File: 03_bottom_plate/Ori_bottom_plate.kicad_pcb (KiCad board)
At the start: 2 copper layers, 278.9 x 76 mm, 81 parts, among them U1 HOLE, U10 HOLE, U11 HOLE, U12 HOLE, U13 HOLE, U14 HOLE, U15 HOLE, U16 HOLE, U17 HOLE, U18 HOLE, U19 HOLE, U2 HOLE, U20 HOLE, U21 HOLE, U22 HOLE, U23 HOLE, U24 HOLE, U25 HOLE, U26 HOLE, U27 HOLE, U28 HOLE, U29 HOLE, U3 HOLE, U30 HOLE, U31 HOLE, U32 HOLE, U33 HOLE, U34 HOLE, U35 HOLE, U36 HOLE, U37 HOLE, U38 HOLE, U39 HOLE, U4 HOLE, U40 HOLE, U41 HOLE, U42 HOLE, U43 HOLE, U44 HOLE, U45 HOLE, U46 HOLE, U47 HOLE, U48 HOLE, U49 HOLE, U5 HOLE, U50 HOLE, U51 HOLE, U52 HOLE, U53 HOLE, U54 HOLE, U57 HOLE, U6 HOLE, U61 HOLE, U7 HOLE, U8 HOLE, U9 HOLE

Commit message: remove a column
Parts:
- removed H21, H22, H23: MountingHole, acheron_Hardware:MouseBite_IPC7351
- removed H24, H25: MountingHole, random-keyboard-parts:Generic-Mounthole
- removed U50, U51, U52, U54: HOLE, Keeb_footprints:MX100_outline
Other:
- board size 278.9 x 76 mm -> 253.5 x 76 mm

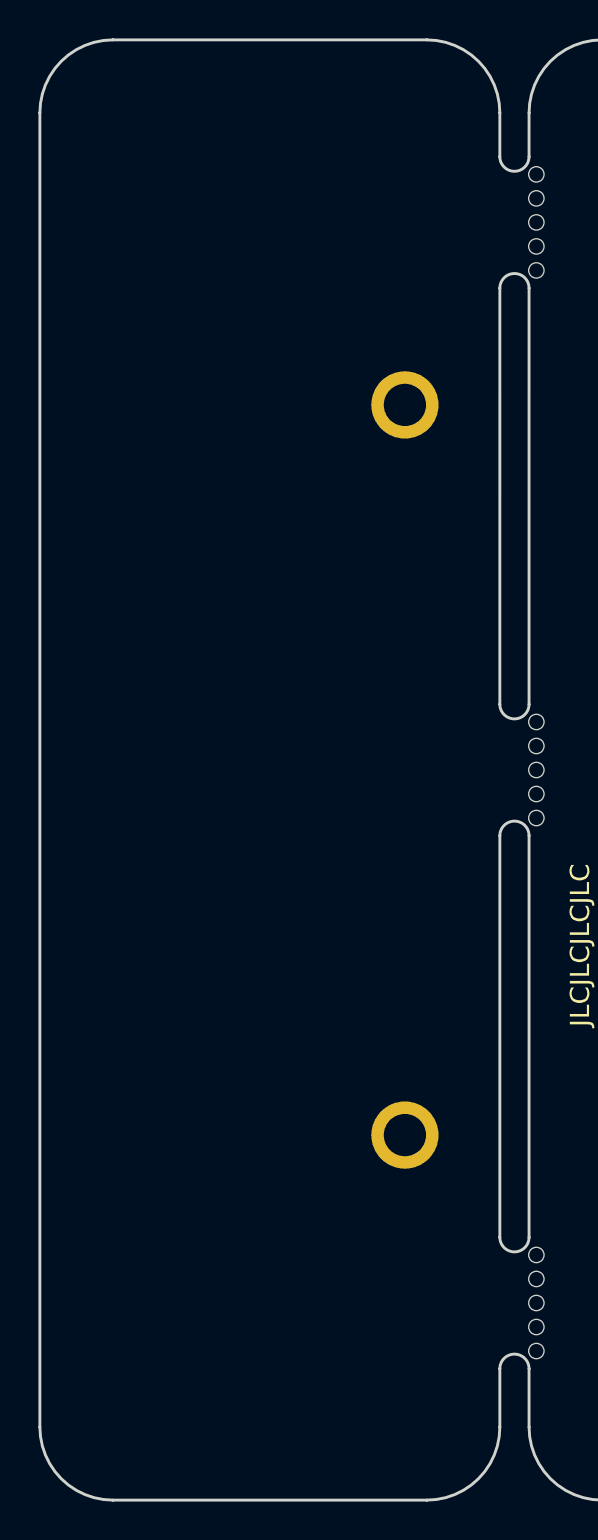
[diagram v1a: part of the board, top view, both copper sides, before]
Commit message: Moved macro column a tiny bit
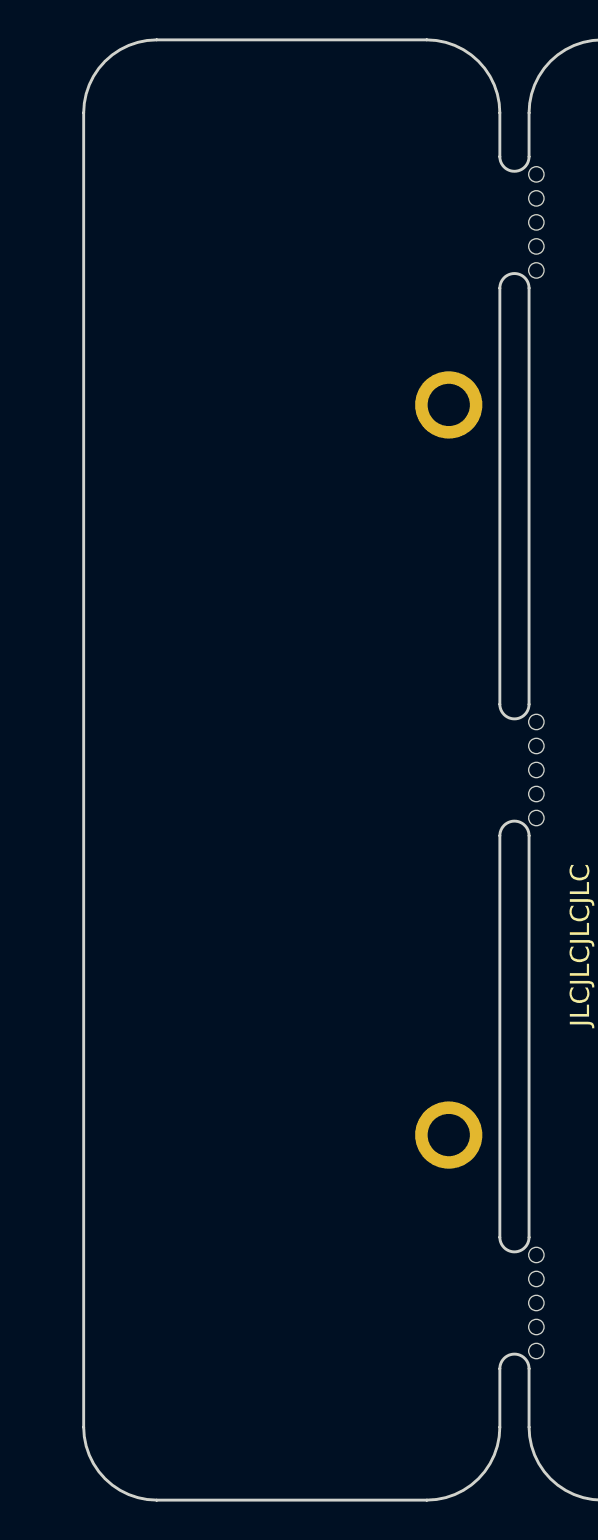
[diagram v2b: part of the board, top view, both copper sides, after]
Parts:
- moved H16 2.28 mm to (141.7, 59.7)
- moved H7 2.28 mm to (141.7, 97.7)
- moved U49 2.28 mm to (132.2, 50.2)
- moved U53 2.28 mm to (132.2, 69.2)
- moved U57 2.28 mm to (132.2, 88.2)
- moved U61 2.28 mm to (132.2, 107.2)
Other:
- board size 253.5 x 76 mm -> 251.2 x 76 mm

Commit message: 19.05mm spacing; move macro column to right side
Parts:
- removed H1, H2, H3, H4, H5, H6: MountingHole, random-keyboard-parts:Generic-Mounthole
- added D1: DIODE, Keeb_footprints:D_SOD-123_modified, F.Cu at (389.4, 59.5)
- moved U53 257.1 mm to (389.4, 69.0)
- moved U49 257.1 mm to (389.3, 50.0)
- moved U57 257.1 mm to (389.3, 88.1)
- moved U61 257.1 mm to (389.3, 107.2)
- moved H16 238.1 mm to (379.8, 59.5)
- moved H7 238.1 mm to (379.8, 97.7)
- moved H19 228.7 mm to (375.0, 107.2)
- moved H18 228.7 mm to (375.0, 50.0)
- moved H20 228.7 mm to (375.0, 78.6)
- moved H17 1.83 mm to (203.6, 50.0)
- moved U12 1.11 mm to (365.5, 50.0)
- moved U24 1.11 mm to (365.5, 69.1)
- moved U36 1.10 mm to (365.5, 88.1)
- moved U48 1.10 mm to (365.5, 107.2)
- moved U11 1.06 mm to (346.5, 50.0)
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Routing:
- net GND: track 0.00 -> 6.09 mm, vias 0 -> 2
- added copper zone on B.Cu, net GND
- added copper zone on F.Cu, net GND
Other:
- board size 251.2 x 76 mm -> 252.4 x 76.2 mm

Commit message: Updated firmware
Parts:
- added H1: MountingHole, random-keyboard-parts:Generic-Mounthole, F.Cu at (165.5, 39.9)
- added H2: MountingHole, random-keyboard-parts:Generic-Mounthole, F.Cu at (165.5, 117.3)
- added H21: MountingHole, random-keyboard-parts:Generic-Mounthole, F.Cu at (389.4, 39.9)
- added H22: MountingHole, random-keyboard-parts:Generic-Mounthole, F.Cu at (389.4, 117.3)
- added H3: MountingHole, random-keyboard-parts:Generic-Mounthole, F.Cu at (260.8, 39.9)
- added H4: MountingHole, random-keyboard-parts:Generic-Mounthole, F.Cu at (260.8, 117.3)
- added H5: MountingHole, random-keyboard-parts:Generic-Mounthole, F.Cu at (337.0, 39.9)
- added H6: MountingHole, random-keyboard-parts:Generic-Mounthole, F.Cu at (337.0, 117.3)
- moved H9 0.14 mm to (165.5, 59.5)
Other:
- board size 252.4 x 76.2 mm -> 252.4 x 82.2 mm
- rule pad_to_mask_clearance: 0.051 -> 0

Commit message: added different plate mounts
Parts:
- removed the H10 at (222.6, 59.5)
- removed the H11 at (222.6, 97.6)
- removed H12, H13, H14, H15, H16, H17, H21, H22: MountingHole, random-keyboard-parts:Generic-Mounthole
- removed the H9 at (165.5, 59.5)
- moved H8 224.7 mm to (389.4, 117.3)
- moved H7 58.6 mm to (389.4, 39.9)
- renumbered H19 to H10, H20 to H11, H18 to H9

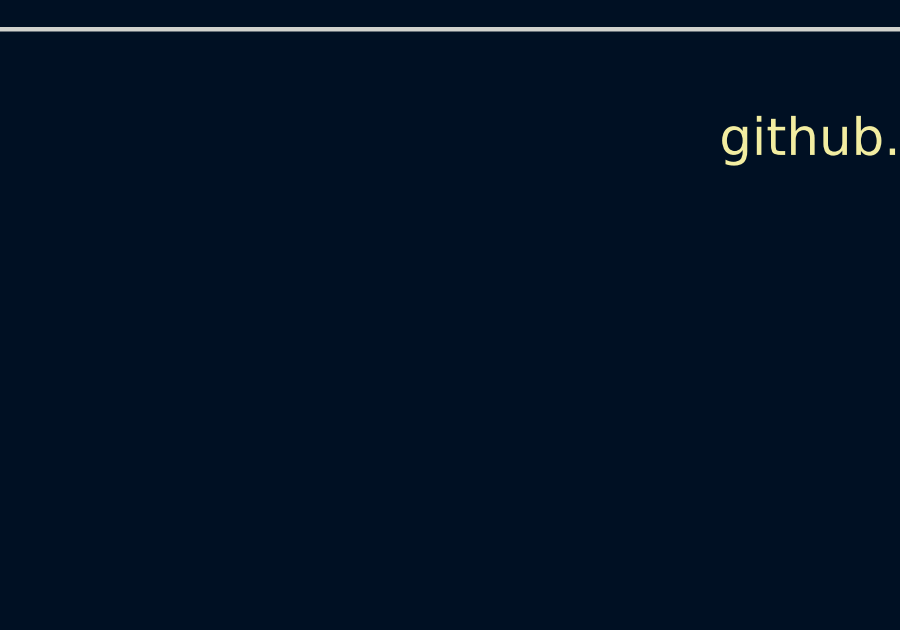
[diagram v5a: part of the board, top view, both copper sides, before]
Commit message: modify top plate
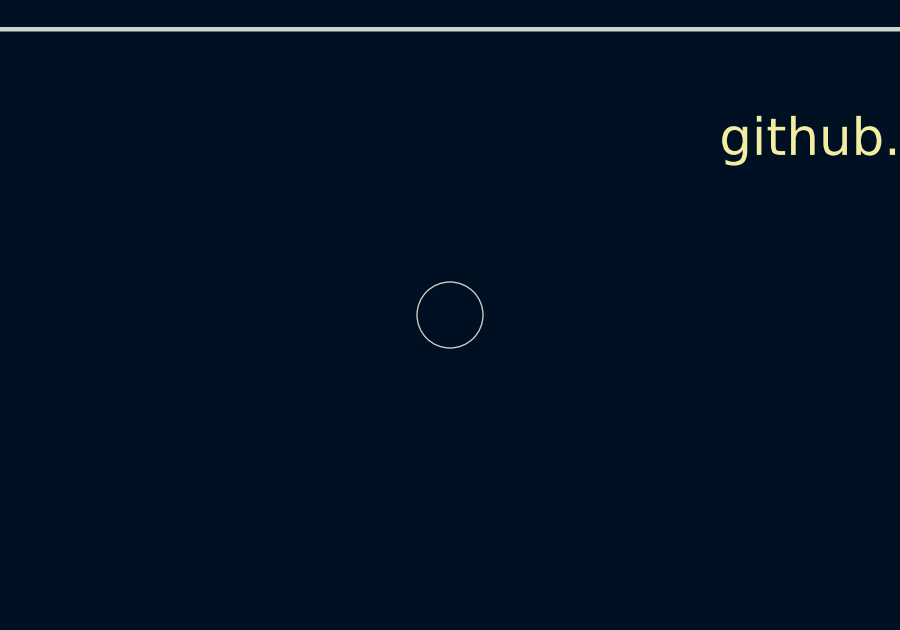
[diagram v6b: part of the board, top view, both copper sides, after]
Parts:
- added H12: MountingHole, random-keyboard-parts:Generic-Mounthole, F.Cu at (203.6, 50.0)
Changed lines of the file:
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@@
     (tracks 4)
     (zones 0)
-    (modules 64)
+    (modules 65)
     (nets 3)
   )
@@
     (mod_text_size 1 1)
     (mod_text_width 0.15)
-    (pad_size 0.1 0.1)
-    (pad_drill 0)
+    (pad_size 2.2 2.2)
+    (pad_drill 2.2)
     (pad_to_mask_clearance 0)
     (aux_axis_origin 279.82341 78.56884)
@@
   )
   (module random-keyboard-parts:Generic-Mounthole (layer F.Cu)
+    (at 203.623474 49.993944)
+    (attr virtual)
+    (fp_text reference H12 (at 0 2) (layer Dwgs.User)
+      (effects (font (size 1 1) (thickness 0.15)))
+    )
+    (fp_text value MountingHole (at 0 -2) (layer Dwgs.User)
+      (effects (font (size 1 1) (thickness 0.15)))
+    )
+    (pad "" np_thru_hole circle (at 0 0) (size 2.2 2.2) (drill 2.2) (layers *.Cu *.Mask))
+  )
+  (module random-keyboard-parts:Generic-Mounthole (layer F.Cu)
